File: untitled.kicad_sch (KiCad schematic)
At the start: 1 part

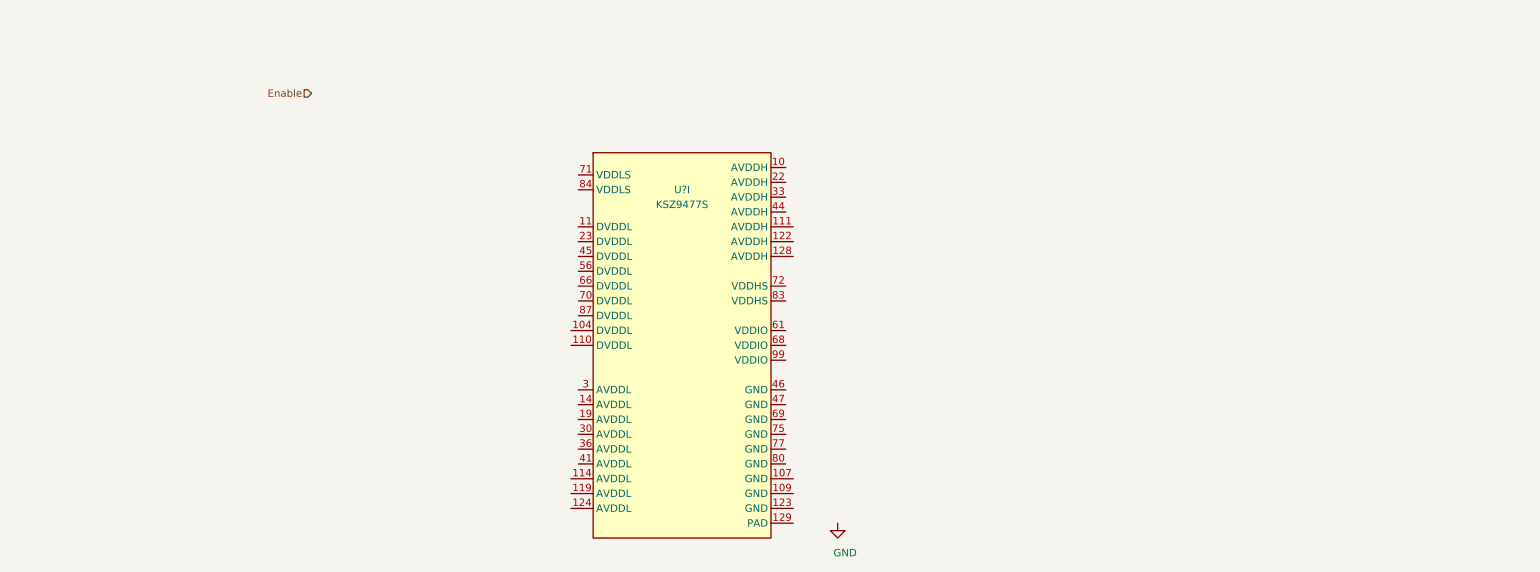
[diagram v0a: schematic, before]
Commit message: Add power supply to the KSZ9477S
Signed-off-by: Oleksij Rempel <linux@rempel-privat.de>
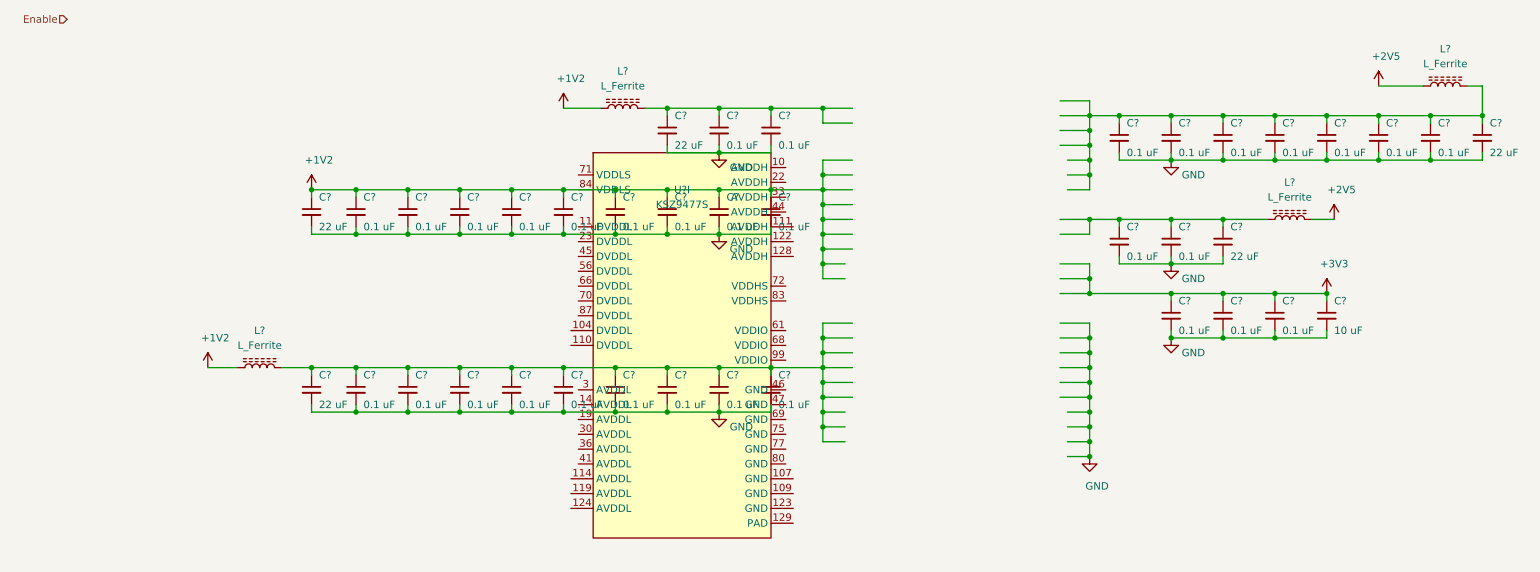
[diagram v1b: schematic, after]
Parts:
- added C? (x32): 0.1 uF, symbol Device:C_Small
- added C? (x5): 22 uF, symbol Device:C_Small
- added C?: 10 uF, symbol Device:C_Small
- added L? (x4): L_Ferrite, symbol Device:L_Ferrite
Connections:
- net GND: now also C?.2, C?.2, C?.2, C?.2, C?.2, C?.2, C?.2, C?.2, C?.2, C?.2, C?.2, C?.2, C?.2, C?.2, C?.2, C?.2, C?.2, C?.2, C?.2, C?.2, C?.2, C?.2, C?.2, C?.2, C?.2, C?.2, C?.2, C?.2, C?.2, C?.2, C?.2, C?.2, C?.2, C?.2, C?.2, C?.2, C?.2, C?.2
- new net: C?.1, C?.1, C?.1, C?.1, C?.1, C?.1, C?.1, C?.1, L?.2
- new net: C?.1, C?.1, C?.1, C?.1, C?.1, C?.1, C?.1, C?.1, C?.1, C?.1, L?.2
- new net: C?.1, C?.1, C?.1, L?.1
- new net: C?.1, C?.1, C?.1, L?.2
- new net +1V2: C?.1, C?.1, C?.1, C?.1, C?.1, C?.1, C?.1, C?.1, C?.1, C?.1, L?.1, L?.1
- new net +2V5: L?.1, L?.2
- new net +3V3: C?.1, C?.1, C?.1, C?.1

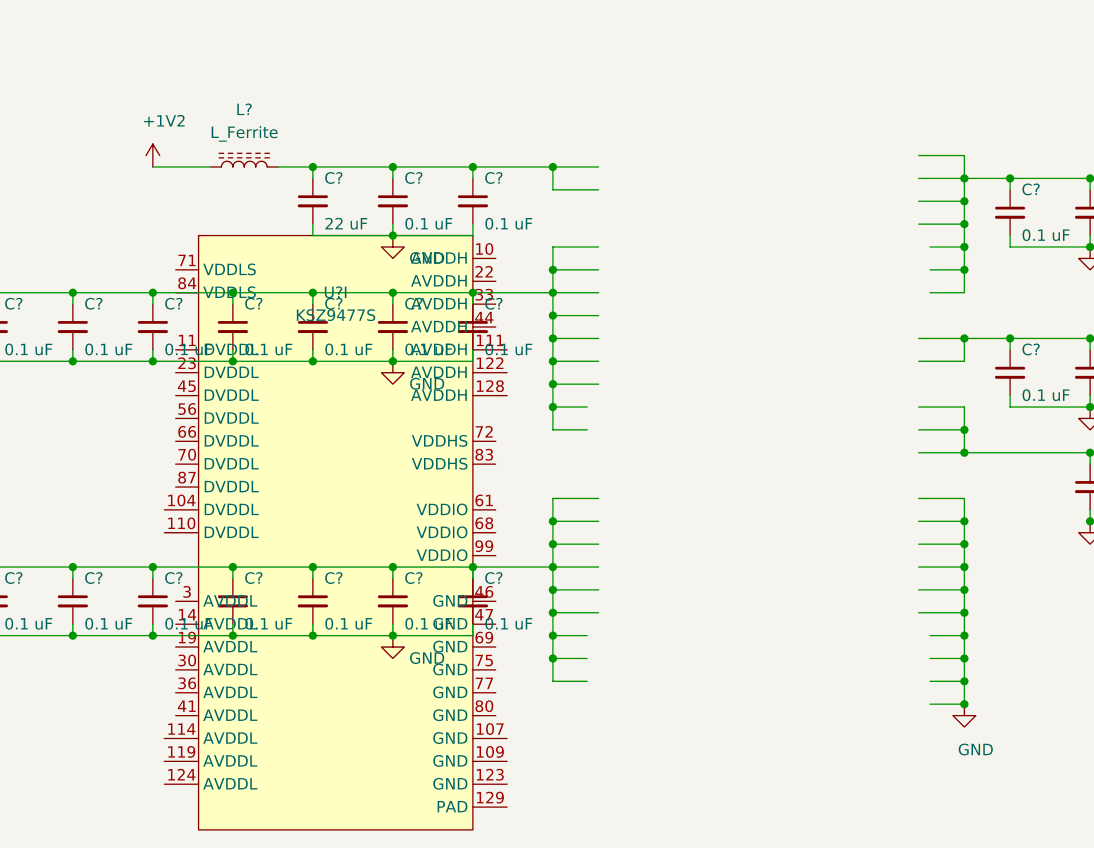
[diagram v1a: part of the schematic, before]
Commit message: ksz9477s: update location for anotations
Signed-off-by: Oleksij Rempel <linux@rempel-privat.de>
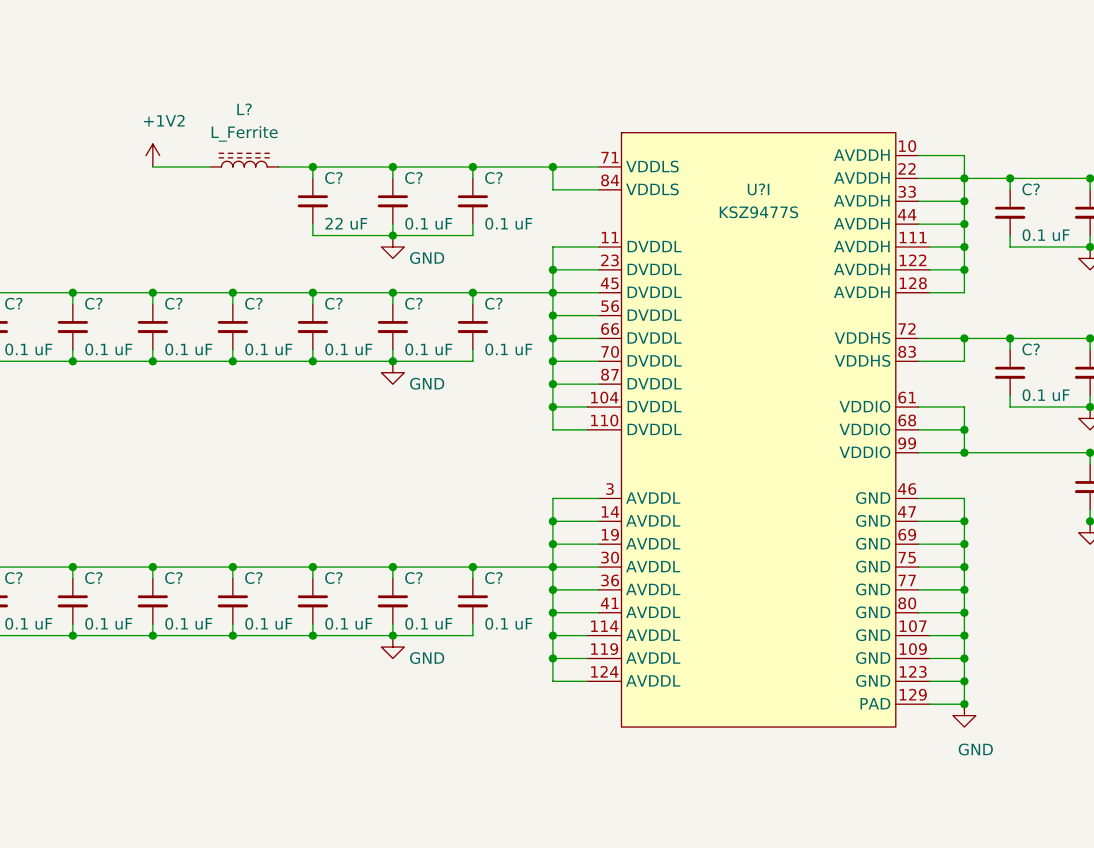
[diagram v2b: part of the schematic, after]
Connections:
- net +1V2: now also U?.104 (DVDDL), U?.11 (DVDDL), U?.110 (DVDDL), U?.23 (DVDDL), U?.45 (DVDDL), U?.56 (DVDDL), U?.66 (DVDDL), U?.70 (DVDDL), U?.87 (DVDDL)
- net +3V3: now also U?.61 (VDDIO), U?.68 (VDDIO), U?.99 (VDDIO)
- net GND: now also U?.107 (GND), U?.109 (GND), U?.123 (GND), U?.129 (PAD), U?.46 (GND), U?.47 (GND), U?.69 (GND), U?.75 (GND), U?.77 (GND), U?.80 (GND)
- net at C?.1, C?.1, C?.1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: now also U?.10 (AVDDH), U?.111 (AVDDH), U?.122 (AVDDH), U?.128 (AVDDH), U?.22 (AVDDH), U?.33 (AVDDH), U?.44 (AVDDH)
- net at C?.1, C?.1, C?.1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: now also U?.114 (AVDDL), U?.119 (AVDDL), U?.124 (AVDDL), U?.14 (AVDDL), U?.19 (AVDDL), U?.3 (AVDDL), U?.30 (AVDDL), U?.36 (AVDDL), U?.41 (AVDDL)
- net at C?.1, C?.1, C?.1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: now also U?.72 (VDDHS), U?.83 (VDDHS)
- net at C?.1, C?.1, C?.1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: now also U?.71 (VDDLS), U?.84 (VDDLS)
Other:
- moved on the sheet: U?I
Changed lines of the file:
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@@
     )
   )
-  (symbol (lib_id "local:KSZ9477S") (at 133.35 76.2 0) (unit 9)
+  (symbol (lib_id "local:KSZ9477S") (at 180.34 64.77 0) (unit 9)
     (in_bom yes) (on_board yes)
-    (property "Reference" "U?" (id 0) (at 133.35 55.88 0))
-    (property "Value" "KSZ9477S" (id 1) (at 133.35 58.42 0))
-    (property "Footprint" "Package_QFP:TQFP-128_14x14mm_P0.4mm" (id 2) (at 117.856 97.282 0)
+    (property "Reference" "U?" (id 0) (at 180.34 44.45 0))
+    (property "Value" "KSZ9477S" (id 1) (at 180.34 46.99 0))
+    (property "Footprint" "Package_QFP:TQFP-128_14x14mm_P0.4mm" (id 2) (at 164.846 85.852 0)
       (effects (font (size 1.27 1.27)) hide)
     )
-    (property "Datasheet" "https://ww1.microchip.com/downloads/en/DeviceDoc/KSZ9477S-Data-Sheet-DS00002392C.pdf" (id 3) (at 132.08 -8.89 0)
+    (property "Datasheet" "https://ww1.microchip.com/downloads/en/DeviceDoc/KSZ9477S-Data-Sheet-DS00002392C.pdf" (id 3) (at 179.07 -20.32 0)
       (effects (font (size 1.27 1.27)) hide)
     )

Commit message: add ports
Signed-off-by: Oleksij Rempel <linux@rempel-privat.de>
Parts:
- removed L? (x4): L_Ferrite, symbol Device:L_Ferrite
- C1, C10, C11, C12, C13, C14, C15, C16, C17, C18, C19, C2, C20, C21, C22, C23, C24, C25, C26, C27, C28, C29, C3, C30, C31, C32, C33, C34, C35, C36, C37, C38, C4, C5, C6, C7, C8, C9: renamed from C?; footprint (none) -> Capacitor_SMD:C_0402_1005Metric_Pad0.74x0.62mm_HandSolder
- gave numbers to parts that had none: 1
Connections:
- net +1V2: now also C10.1, C12.1, C14.1, C15.1, C17.1, C18.1, C2.1, C20.1, C21.1, C23.1, C4.1, C6.1, C8.1, U1.114 (AVDDL), U1.119 (AVDDL), U1.124 (AVDDL), U1.14 (AVDDL), U1.19 (AVDDL), U1.3 (AVDDL), U1.30 (AVDDL), U1.36 (AVDDL), U1.41 (AVDDL), U1.71 (VDDLS), U1.84 (VDDLS)
- net +2V5: now also C24.1, C25.1, C26.1, C27.1, C29.1, C30.1, C32.1, C34.1, C36.1, C37.1, C38.1, U1.10 (AVDDH), U1.111 (AVDDH), U1.122 (AVDDH), U1.128 (AVDDH), U1.22 (AVDDH), U1.33 (AVDDH), U1.44 (AVDDH), U1.72 (VDDHS), U1.83 (VDDHS)

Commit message: add TQFP-128_14x14mm_P0.4mm_EP10x10mm_ThermalVias footprint
and assign it to the ksz chip

Signed-off-by: Oleksij Rempel <linux@rempel-privat.de>
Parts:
- U1: footprint Package_QFP:TQFP-128_14x14mm_P0.4mm -> footprints:TQFP-128_14x14mm_P0.4mm_EP10x10mm_ThermalVias
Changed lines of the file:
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@@
     (property "Reference" "U1" (id 0) (at 180.34 44.45 0))
     (property "Value" "KSZ9477S" (id 1) (at 180.34 46.99 0))
-    (property "Footprint" "Package_QFP:TQFP-128_14x14mm_P0.4mm" (id 2) (at 164.846 85.852 0)
+    (property "Footprint" "footprints:TQFP-128_14x14mm_P0.4mm_EP10x10mm_ThermalVias" (id 2) (at 164.846 85.852 0)
       (effects (font (size 1.27 1.27)) hide)
     )

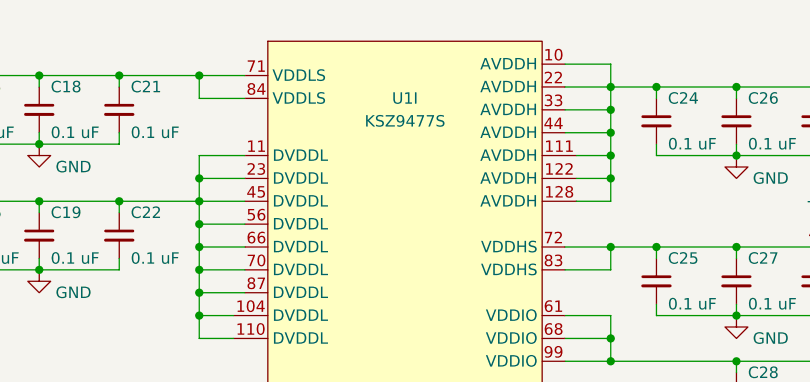
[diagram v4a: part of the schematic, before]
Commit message: update pin naming. use _P/_N to allow optiomisation for differential signal
Signed-off-by: Oleksij Rempel <linux@rempel-privat.de>
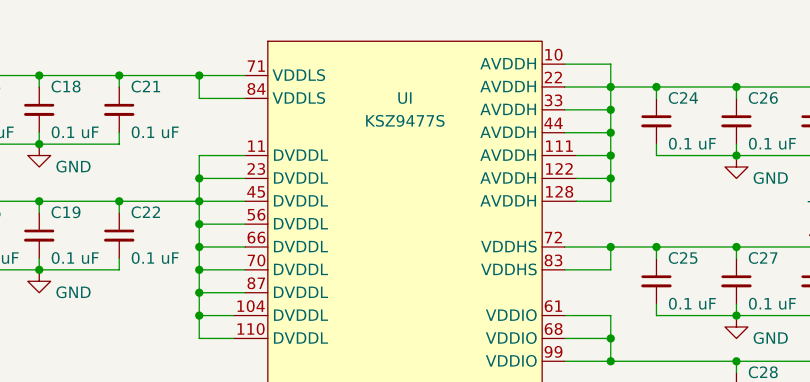
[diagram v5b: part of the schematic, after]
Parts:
- renumbered U1 to U
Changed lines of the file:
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@@
-(kicad_sch (version 20201015) (generator eeschema)
+(kicad_sch (version 20210126) (generator eeschema)
   (paper "A4")
   (junction (at 69.85 55.88) (diameter 0.9144) (color 0 0 0 0))
@@
       (effects (font (size 1.27 1.27)) hide)
     )
+    (pin "1")
   )
   (symbol (lib_id "power:+1V2") (at 69.85 86.36 0) (unit 1)
@@
       (effects (font (size 1.27 1.27)) hide)
     )
+    (pin "1")
   )
   (symbol (lib_id "power:+1V2") (at 130.81 41.91 0) (unit 1)
@@
       (effects (font (size 1.27 1.27)) hide)
     )
+    (pin "1")
   )
   (symbol (lib_id "power:+2V5") (at 226.06 60.96 0) (unit 1)
@@
       (effects (font (size 1.27 1.27)) hide)
     )
+    (pin "1")
   )
   (symbol (lib_id "power:+3V3") (at 243.84 73.66 0) (unit 1)
@@
       (effects (font (size 1.27 1.27)) hide)
     )
+    (pin "1")
   )
   (symbol (lib_id "power:+2V5") (at 270.51 43.18 0) (unit 1)
@@
       (effects (font (size 1.27 1.27)) hide)
     )
+    (pin "1")
   )
   (symbol (lib_id "power:GND") (at 139.7 49.53 0) (unit 1)
@@
       (effects (font (size 1.27 1.27)) hide)
     )
+    (pin "1")
   )
   (symbol (lib_id "power:GND") (at 139.7 63.5 0) (unit 1)
@@
       (effects (font (size 1.27 1.27)) hide)
     )
+    (pin "1")
   )
   (symbol (lib_id "power:GND") (at 139.7 93.98 0) (unit 1)
@@
       (effects (font (size 1.27 1.27)) hide)
     )
+    (pin "1")
   )
   (symbol (lib_id "power:GND") (at 203.2 101.6 0) (unit 1)
@@
       (effects (font (size 1.27 1.27)) hide)
     )
+    (pin "1")
   )
   (symbol (lib_id "power:GND") (at 217.17 50.8 0) (unit 1)
@@
       (effects (font (size 1.27 1.27)) hide)
     )
+    (pin "1")
   )
   (symbol (lib_id "power:GND") (at 217.17 68.58 0) (unit 1)
@@
       (effects (font (size 1.27 1.27)) hide)
     )
+    (pin "1")
   )
   (symbol (lib_id "power:GND") (at 217.17 81.28 0) (unit 1)
@@
       (effects (font (size 1.27 1.27)) hide)
     )
+    (pin "1")
   )
   (symbol (lib_id "Device:C_Small") (at 69.85 59.69 0) (unit 1)
@@
       (effects (font (size 1.27 1.27)) hide)
     )
+    (pin "1")
+    (pin "2")
   )
   (symbol (lib_id "Device:C_Small") (at 69.85 90.17 0) (unit 1)
@@
       (effects (font (size 1.27 1.27)) hide)
     )
+    (pin "1")
+    (pin "2")
   )
   (symbol (lib_id "Device:C_Small") (at 77.47 59.69 0) (unit 1)
@@
       (effects (font (size 1.27 1.27)) hide)
     )
+    (pin "1")
+    (pin "2")
   )
   (symbol (lib_id "Device:C_Small") (at 77.47 90.17 0) (unit 1)
@@
       (effects (font (size 1.27 1.27)) hide)
     )
+    (pin "1")
+    (pin "2")
   )
   (symbol (lib_id "Device:C_Small") (at 86.36 59.69 0) (unit 1)
@@
       (effects (font (size 1.27 1.27)) hide)
     )
+    (pin "1")
+    (pin "2")
   )
   (symbol (lib_id "Device:C_Small") (at 86.36 90.17 0) (unit 1)
@@
       (effects (font (size 1.27 1.27)) hide)
     )
+    (pin "1")
+    (pin "2")
   )
   (symbol (lib_id "Device:C_Small") (at 95.25 59.69 0) (unit 1)
@@
       (effects (font (size 1.27 1.27)) hide)
     )
+    (pin "1")
+    (pin "2")
   )
   (symbol (lib_id "Device:C_Small") (at 95.25 90.17 0) (unit 1)
@@
       (effects (font (size 1.27 1.27)) hide)
     )
+    (pin "1")
+    (pin "2")
   )
   (symbol (lib_id "Device:C_Small") (at 104.14 59.69 0) (unit 1)
@@
       (effects (font (size 1.27 1.27)) hide)
     )
+    (pin "1")
+    (pin "2")
   )
   (symbol (lib_id "Device:C_Small") (at 104.14 90.17 0) (unit 1)
@@
       (effects (font (size 1.27 1.27)) hide)
     )
+    (pin "1")
+    (pin "2")
   )
   (symbol (lib_id "Device:C_Small") (at 113.03 59.69 0) (unit 1)
@@
       (effects (font (size 1.27 1.27)) hide)
     )
+    (pin "1")
+    (pin "2")
   )
   (symbol (lib_id "Device:C_Small") (at 113.03 90.17 0) (unit 1)
@@
       (effects (font (size 1.27 1.27)) hide)
     )
+    (pin "1")
+    (pin "2")
   )
   (symbol (lib_id "Device:C_Small") (at 121.92 59.69 0) (unit 1)
@@
       (effects (font (size 1.27 1.27)) hide)
     )
+    (pin "1")
+    (pin "2")
   )
   (symbol (lib_id "Device:C_Small") (at 121.92 90.17 0) (unit 1)
@@
       (effects (font (size 1.27 1.27)) hide)
     )
+    (pin "1")
+    (pin "2")
   )
   (symbol (lib_id "Device:C_Small") (at 130.81 45.72 0) (unit 1)
@@
       (effects (font (size 1.27 1.27)) hide)
     )
+    (pin "1")
+    (pin "2")
   )
   (symbol (lib_id "Device:C_Small") (at 130.81 59.69 0) (unit 1)
@@
       (effects (font (size 1.27 1.27)) hide)
     )
+    (pin "1")
+    (pin "2")
   )
   (symbol (lib_id "Device:C_Small") (at 130.81 90.17 0) (unit 1)
@@
       (effects (font (size 1.27 1.27)) hide)
     )
+    (pin "1")
+    (pin "2")
   )
   (symbol (lib_id "Device:C_Small") (at 139.7 45.72 0) (unit 1)
@@
       (effects (font (size 1.27 1.27)) hide)
     )
+    (pin "1")
+    (pin "2")
   )
   (symbol (lib_id "Device:C_Small") (at 139.7 59.69 0) (unit 1)
@@
       (effects (font (size 1.27 1.27)) hide)
     )
+    (pin "1")
+    (pin "2")
   )
   (symbol (lib_id "Device:C_Small") (at 139.7 90.17 0) (unit 1)
@@
       (effects (font (size 1.27 1.27)) hide)
     )
+    (pin "1")
+    (pin "2")
   )
   (symbol (lib_id "Device:C_Small") (at 148.59 45.72 0) (unit 1)
@@
       (effects (font (size 1.27 1.27)) hide)
     )
+    (pin "1")
+    (pin "2")
   )
   (symbol (lib_id "Device:C_Small") (at 148.59 59.69 0) (unit 1)
@@
       (effects (font (size 1.27 1.27)) hide)
     )
+    (pin "1")
+    (pin "2")
   )
   (symbol (lib_id "Device:C_Small") (at 148.59 90.17 0) (unit 1)
@@
       (effects (font (size 1.27 1.27)) hide)
     )
+    (pin "1")
+    (pin "2")
   )
   (symbol (lib_id "Device:C_Small") (at 208.28 46.99 0) (unit 1)
@@
       (effects (font (size 1.27 1.27)) hide)
     )
+    (pin "1")
+    (pin "2")
   )
   (symbol (lib_id "Device:C_Small") (at 208.28 64.77 0) (unit 1)
@@
       (effects (font (size 1.27 1.27)) hide)
     )
+    (pin "1")
+    (pin "2")
   )
   (symbol (lib_id "Device:C_Small") (at 217.17 46.99 0) (unit 1)
@@
       (effects (font (size 1.27 1.27)) hide)
     )
+    (pin "1")
+    (pin "2")
   )
   (symbol (lib_id "Device:C_Small") (at 217.17 64.77 0) (unit 1)
@@
       (effects (font (size 1.27 1.27)) hide)
     )
+    (pin "1")
+    (pin "2")
   )
   (symbol (lib_id "Device:C_Small") (at 217.17 77.47 0) (unit 1)
@@
       (effects (font (size 1.27 1.27)) hide)
     )
+    (pin "1")
+    (pin "2")
   )
   (symbol (lib_id "Device:C_Small") (at 226.06 46.99 0) (unit 1)
@@
       (effects (font (size 1.27 1.27)) hide)
     )
+    (pin "1")
+    (pin "2")
   )
   (symbol (lib_id "Device:C_Small") (at 226.06 64.77 0) (unit 1)
@@
       (effects (font (size 1.27 1.27)) hide)
     )
+    (pin "1")
+    (pin "2")
   )
   (symbol (lib_id "Device:C_Small") (at 226.06 77.47 0) (unit 1)
@@
       (effects (font (size 1.27 1.27)) hide)
     )
+    (pin "1")
+    (pin "2")
   )
   (symbol (lib_id "Device:C_Small") (at 234.95 46.99 0) (unit 1)
@@
       (effects (font (size 1.27 1.27)) hide)
     )
+    (pin "1")
+    (pin "2")
   )
   (symbol (lib_id "Device:C_Small") (at 234.95 77.47 0) (unit 1)
@@
       (effects (font (size 1.27 1.27)) hide)
     )
+    (pin "1")
+    (pin "2")
   )
   (symbol (lib_id "Device:C_Small") (at 243.84 46.99 0) (unit 1)
@@
       (effects (font (size 1.27 1.27)) hide)
     )
+    (pin "1")
+    (pin "2")
   )
   (symbol (lib_id "Device:C_Small") (at 243.84 77.47 0) (unit 1)
@@
       (effects (font (size 1.27 1.27)) hide)
     )
+    (pin "1")
+    (pin "2")
   )
   (symbol (lib_id "Device:C_Small") (at 252.73 46.99 0) (unit 1)
@@
       (effects (font (size 1.27 1.27)) hide)
     )
+    (pin "1")
+    (pin "2")
   )
   (symbol (lib_id "Device:C_Small") (at 261.62 46.99 0) (unit 1)
@@
       (effects (font (size 1.27 1.27)) hide)
     )
+    (pin "1")
+    (pin "2")
   )
   (symbol (lib_id "Device:C_Small") (at 270.51 46.99 0) (unit 1)
@@
       (effects (font (size 1.27 1.27)) hide)
     )
+    (pin "1")
+    (pin "2")
   )
   (symbol (lib_id "local:KSZ9477S") (at 180.34 64.77 0) (unit 9)
     (in_bom yes) (on_board yes)
-    (property "Reference" "U1" (id 0) (at 180.34 44.45 0))
+    (property "Reference" "U" (id 0) (at 180.34 44.45 0))
     (property "Value" "KSZ9477S" (id 1) (at 180.34 46.99 0))
     (property "Footprint" "footprints:TQFP-128_14x14mm_P0.4mm_EP10x10mm_ThermalVias" (id 2) (at 164.846 85.852 0)
@@
       (effects (font (size 1.27 1.27)) hide)
     )
+    (pin "46")
+    (pin "61")
+    (pin "10")
+    (pin "3")
+    (pin "11")
+    (pin "71")
+    (pin "72")
+    (pin "68")
+    (pin "99")
+    (pin "22")
+    (pin "33")
+    (pin "44")
+    (pin "111")
+    (pin "122")
+    (pin "128")
+    (pin "14")
+    (pin "19")
+    (pin "30")
+    (pin "36")
+    (pin "41")
+    (pin "114")
+    (pin "119")
+    (pin "124")
+    (pin "23")
+    (pin "45")
+    (pin "56")
+    (pin "66")
+    (pin "70")
+    (pin "87")
+    (pin "104")
+    (pin "110")
+    (pin "84")
+    (pin "83")
+    (pin "47")
+    (pin "69")
+    (pin "75")
+    (pin "77")
+    (pin "80")
+    (pin "107")
+    (pin "109")
+    (pin "123")
+    (pin "129")
   )
 )
